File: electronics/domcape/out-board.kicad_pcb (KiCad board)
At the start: 2 copper layers, 20.3 x 32 mm, 6 parts, among them IC1 PC817, P1 CONN_01X03, P2 CONN_01X04, Q1 IRF540N

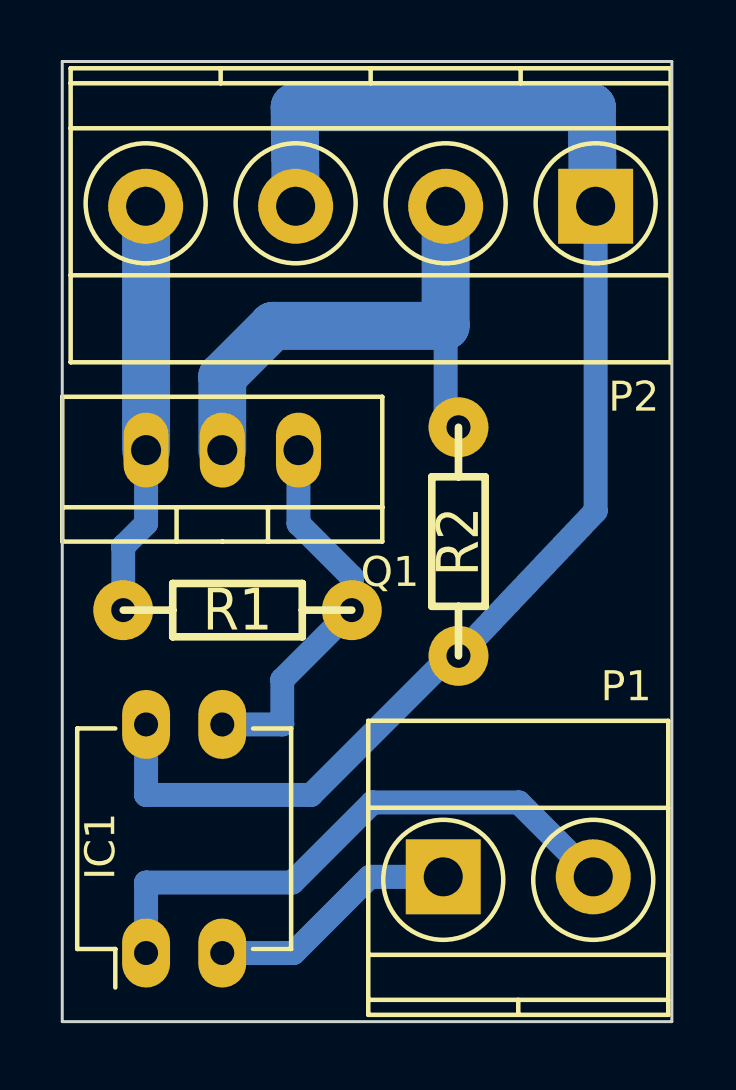
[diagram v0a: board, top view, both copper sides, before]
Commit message: out-board circuit corrections
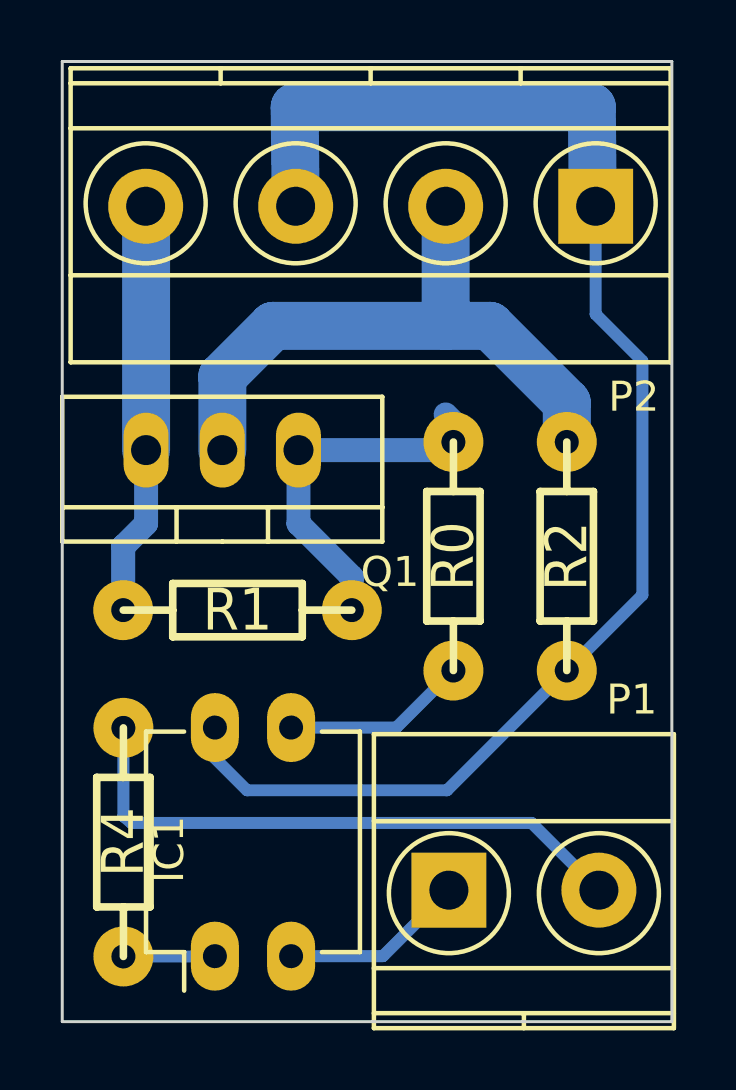
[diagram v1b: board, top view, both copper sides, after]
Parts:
- added R0: 33K, custom:RC03, F.Cu at (149.7, 57.6)
- added R4: 1.2k, custom:RC03, F.Cu at (138.7, 67.2)
- R1: value 4K7 -> 15k
- moved R2 3.64 mm to (153.5, 57.6)
- moved IC1 2.30 mm to (141.7, 71.0)
- moved P1 0.48 mm to (149.5, 68.8)
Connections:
- P1 pad 2: Net-(IC1-Pad1) -> Net-(P1-Pad2)
- Q1 pad 1: Net-(IC1-Pad3) -> Net-(Q1-Pad1)
- R1 pad 1: Net-(IC1-Pad3) -> Net-(Q1-Pad1)
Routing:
- net Net-(P1-Pad2): track 0.00 -> 19.8 mm
- net Net-(IC1-Pad1): track 19.4 -> 3.05 mm
- net Net-(Q1-Pad1): track 0.00 -> 12.6 mm
- net Net-(IC1-Pad3): track 12.8 -> 6.48 mm
- net /OUT_1: track 18.1 -> 21.0 mm
- net Net-(IC1-Pad2): track 8.42 -> 6.55 mm
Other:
- net class signal added: clearance 0.4, trace_width 0.4, via_dia 0.6, via_drill 0.4
